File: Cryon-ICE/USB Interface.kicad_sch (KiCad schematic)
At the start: 50 parts, among them J302 10155435-00011LF, Q301 DMG1012T, U301 PTN5150AHXMP, U302 USB3340-EZK-TR, U303 TPS2051BDR, Y301 12.88481

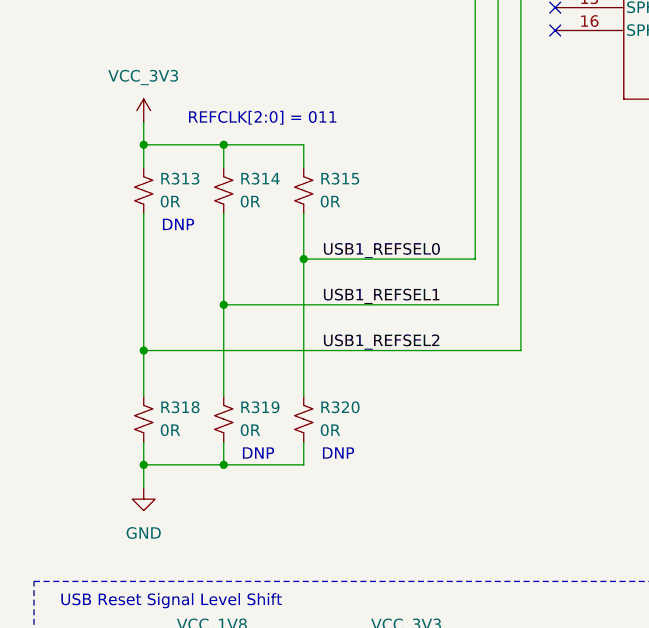
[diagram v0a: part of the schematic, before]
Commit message: Added micro-sd to schematic
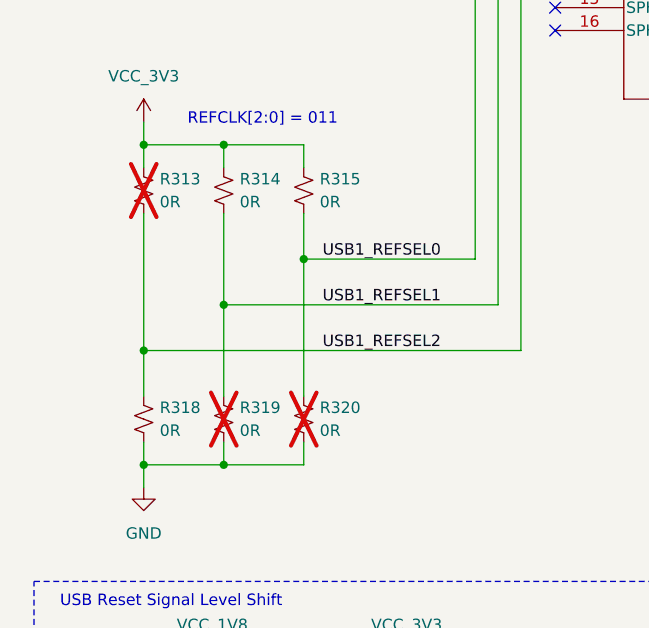
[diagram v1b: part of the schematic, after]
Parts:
- R313, R319, R320: now not fitted
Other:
- note removed: "DNP"
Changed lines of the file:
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@@
 		)
 	)
-	(text "DNP"
-		(exclude_from_sim no)
-		(at 74.93 200.914 0)
-		(effects
-			(font
-				(size 1.27 1.27)
-				(color 0 0 0 1)
-			)
-		)
-	)
 	(text "27MHz"
 		(exclude_from_sim no)
@@
 		)
 	)
-	(text "DNP"
-		(exclude_from_sim no)
-		(at 66.04 175.514 0)
-		(effects
-			(font
-				(size 1.27 1.27)
-				(color 0 0 0 1)
-			)
-		)
-	)
 	(text "Power Switch"
 		(exclude_from_sim no)
@@
 		)
 	)
-	(text "DNP"
-		(exclude_from_sim no)
-		(at 83.82 200.914 0)
-		(effects
-			(font
-				(size 1.27 1.27)
-				(color 0 0 0 1)
-			)
-		)
-	)
 	(junction
 		(at 195.58 40.64)
@@
 		(on_board yes)
 		(in_pos_files yes)
-		(dnp no)
+		(dnp yes)
 		(property "Reference" "R313"
 			(at 64.008 170.18 0)
@@
 		(on_board yes)
 		(in_pos_files yes)
-		(dnp no)
+		(dnp yes)
 		(property "Reference" "R320"
 			(at 81.788 195.58 0)
@@
 		(on_board yes)
 		(in_pos_files yes)
-		(dnp no)
+		(dnp yes)
 		(property "Reference" "R319"
 			(at 72.898 195.58 0)
